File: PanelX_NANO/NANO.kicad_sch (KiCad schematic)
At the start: 5 parts

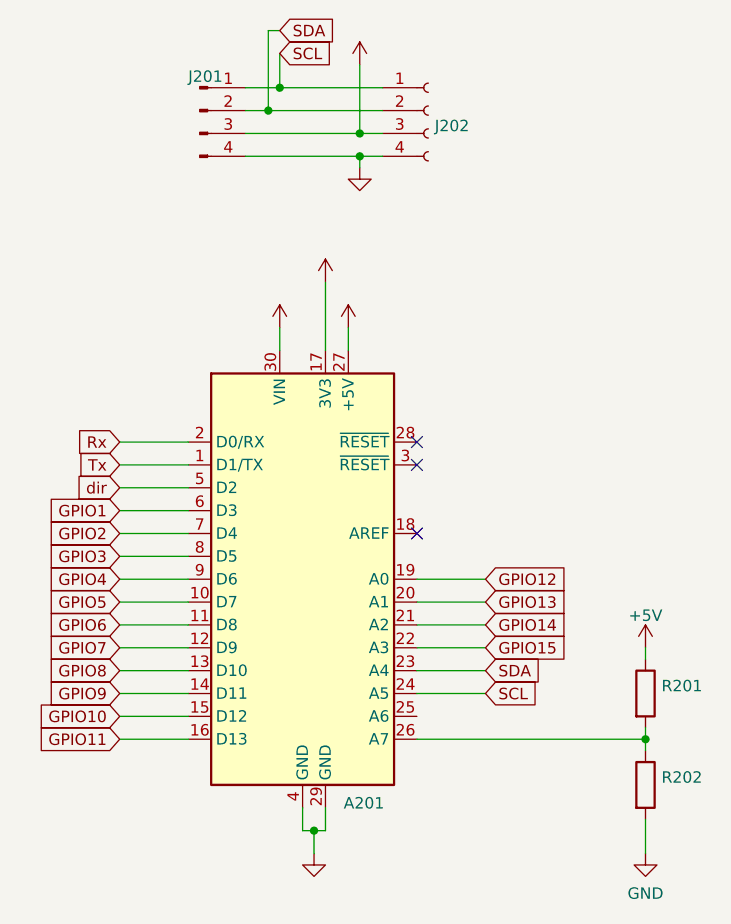
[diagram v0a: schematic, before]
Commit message: Deleted zip files from repo
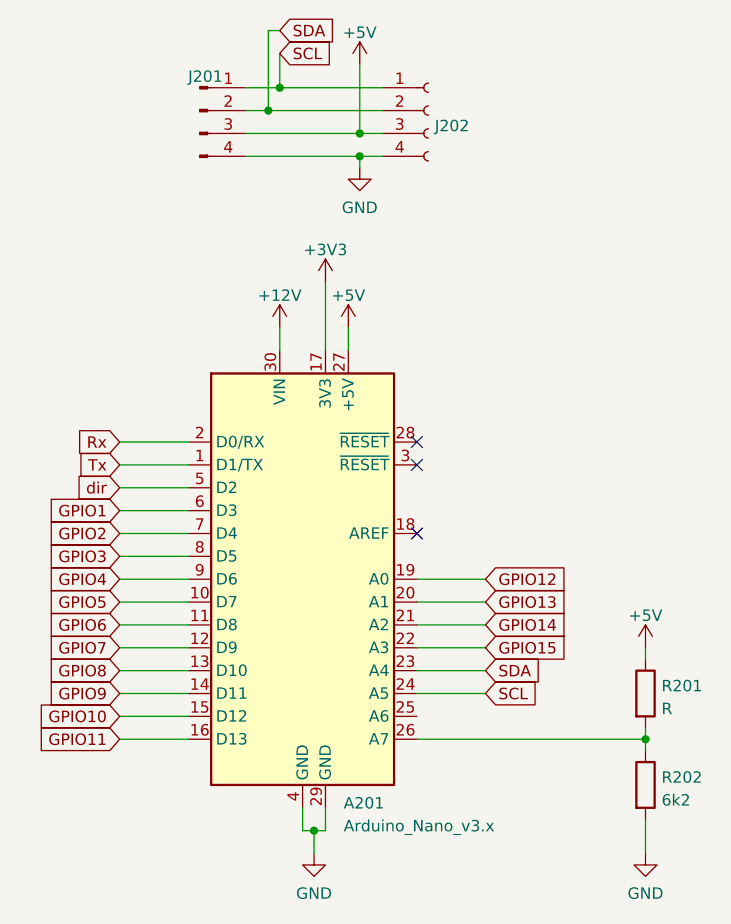
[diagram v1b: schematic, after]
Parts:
- A201: value (none) -> Arduino_Nano_v3.x; footprint (none) -> Module:Arduino_Nano
- J201: value (none) -> Conn_01x04_Male; footprint (none) -> Connector_PinHeader_2.54mm:PinHeader_1x04_P2.54mm_Horizontal
- J202: value (none) -> Conn_01x04_Female; footprint (none) -> Connector_PinSocket_2.54mm:PinSocket_1x04_P2.54mm_Horizontal
- R201: value (none) -> R; footprint (none) -> Resistor_SMD:R_0805_2012Metric_Pad1.20x1.40mm_HandSolder
- R202: value (none) -> 6k2; footprint (none) -> Resistor_SMD:R_0805_2012Metric_Pad1.20x1.40mm_HandSolder
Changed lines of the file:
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@@
       (effects (font (size 1.27 1.27)) (justify left))
     )
-    (property "Value" "" (id 1) (at 175.768 107.1122 0)
-      (effects (font (size 1.27 1.27)) (justify left))
-    )
-    (property "Footprint" "" (id 2) (at 172.212 105.41 90)
+    (property "Value" "R" (id 1) (at 175.768 107.1122 0)
+      (effects (font (size 1.27 1.27)) (justify left))
+    )
+    (property "Footprint" "Resistor_SMD:R_0805_2012Metric_Pad1.20x1.40mm_HandSolder" (id 2) (at 172.212 105.41 90)
       (effects (font (size 1.27 1.27)) hide)
     )
@@
     (in_bom yes) (on_board yes) (fields_autoplaced)
     (property "Reference" "J201" (id 0) (at 125.095 36.861 0))
-    (property "Value" "" (id 1) (at 125.095 36.8609 0)
-      (effects (font (size 1.27 1.27)) hide)
-    )
-    (property "Footprint" "" (id 2) (at 124.46 40.64 0)
+    (property "Value" "Conn_01x04_Male" (id 1) (at 125.095 36.8609 0)
+      (effects (font (size 1.27 1.27)) hide)
+    )
+    (property "Footprint" "Connector_PinHeader_2.54mm:PinHeader_1x04_P2.54mm_Horizontal" (id 2) (at 124.46 40.64 0)
       (effects (font (size 1.27 1.27)) hide)
     )
@@
       (effects (font (size 1.27 1.27)) hide)
     )
-    (property "Value" "" (id 1) (at 140.97 61.1942 0))
+    (property "Value" "+5V" (id 1) (at 140.97 61.1942 0))
     (property "Footprint" "" (id 2) (at 140.97 64.77 0)
       (effects (font (size 1.27 1.27)) hide)
@@
       (effects (font (size 1.27 1.27)) hide)
     )
-    (property "Value" "" (id 1) (at 142.24 51.4334 0))
+    (property "Value" "GND" (id 1) (at 142.24 51.4334 0))
     (property "Footprint" "" (id 2) (at 142.24 46.99 0)
       (effects (font (size 1.27 1.27)) hide)
@@
       (effects (font (size 1.27 1.27)) hide)
     )
-    (property "Value" "" (id 1) (at 142.24 31.9842 0))
+    (property "Value" "+5V" (id 1) (at 142.24 31.9842 0))
     (property "Footprint" "" (id 2) (at 142.24 35.56 0)
       (effects (font (size 1.27 1.27)) hide)
@@
       (effects (font (size 1.27 1.27)) hide)
     )
-    (property "Value" "" (id 1) (at 133.35 61.1942 0))
+    (property "Value" "+12V" (id 1) (at 133.35 61.1942 0))
     (property "Footprint" "" (id 2) (at 133.35 64.77 0)
       (effects (font (size 1.27 1.27)) hide)
@@
       (effects (font (size 1.27 1.27)) (justify left))
     )
-    (property "Value" "" (id 1) (at 140.4494 120.1373 0)
-      (effects (font (size 1.27 1.27)) (justify left))
-    )
-    (property "Footprint" "" (id 2) (at 135.89 92.71 0)
+    (property "Value" "Arduino_Nano_v3.x" (id 1) (at 140.4494 120.1373 0)
+      (effects (font (size 1.27 1.27)) (justify left))
+    )
+    (property "Footprint" "Module:Arduino_Nano" (id 2) (at 135.89 92.71 0)
       (effects (font (size 1.27 1.27) italic) hide)
     )
@@
       (effects (font (size 1.27 1.27)) hide)
     )
-    (property "Value" "" (id 1) (at 137.16 127.6334 0))
+    (property "Value" "GND" (id 1) (at 137.16 127.6334 0))
     (property "Footprint" "" (id 2) (at 137.16 123.19 0)
       (effects (font (size 1.27 1.27)) hide)
@@
       (effects (font (size 1.27 1.27)) (justify left))
     )
-    (property "Value" "" (id 1) (at 175.768 117.2722 0)
-      (effects (font (size 1.27 1.27)) (justify left))
-    )
-    (property "Footprint" "" (id 2) (at 172.212 115.57 90)
+    (property "Value" "6k2" (id 1) (at 175.768 117.2722 0)
+      (effects (font (size 1.27 1.27)) (justify left))
+    )
+    (property "Footprint" "Resistor_SMD:R_0805_2012Metric_Pad1.20x1.40mm_HandSolder" (id 2) (at 172.212 115.57 90)
       (effects (font (size 1.27 1.27)) hide)
     )
@@
       (effects (font (size 1.27 1.27)) (justify left))
     )
-    (property "Value" "" (id 1) (at 150.5712 43.6122 0)
+    (property "Value" "Conn_01x04_Female" (id 1) (at 150.5712 43.6122 0)
       (effects (font (size 1.27 1.27)) (justify left) hide)
     )
-    (property "Footprint" "" (id 2) (at 149.86 40.64 0)
+    (property "Footprint" "Connector_PinSocket_2.54mm:PinSocket_1x04_P2.54mm_Horizontal" (id 2) (at 149.86 40.64 0)
       (effects (font (size 1.27 1.27)) hide)
     )
@@
       (effects (font (size 1.27 1.27)) hide)
     )
-    (property "Value" "" (id 1) (at 138.43 56.1142 0))
+    (property "Value" "+3V3" (id 1) (at 138.43 56.1142 0))
     (property "Footprint" "" (id 2) (at 138.43 59.69 0)
       (effects (font (size 1.27 1.27)) hide)
